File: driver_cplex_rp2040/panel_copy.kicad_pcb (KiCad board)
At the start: 6 copper layers, 40.2 x 40.2 mm, 391 parts, among them J1 Conn_01x05, J2 Conn_01x05, J5 USB_C_Receptacle_USB2.0, U2 AP2112K-3.3, U5 RP2040, U6 W25Q128JVS

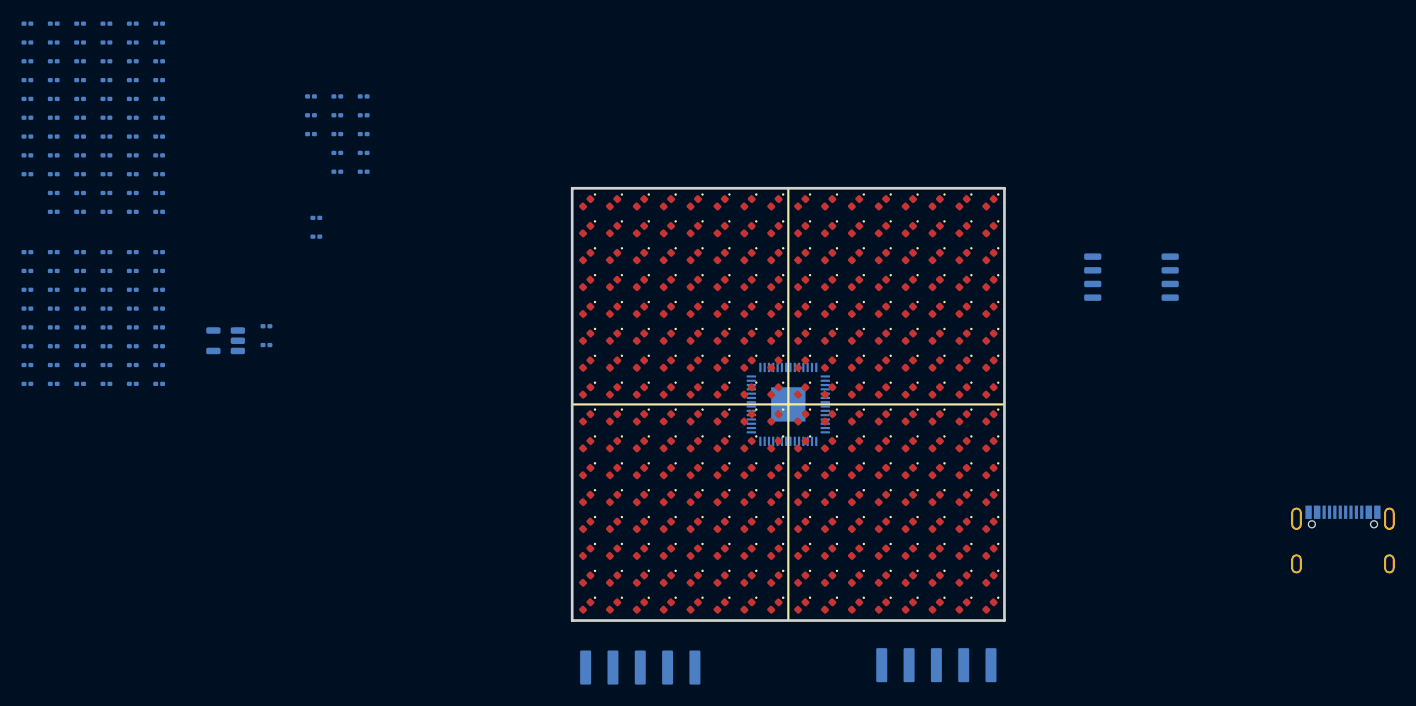
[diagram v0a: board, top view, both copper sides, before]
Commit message: Added charlie plexed version of single panel design.
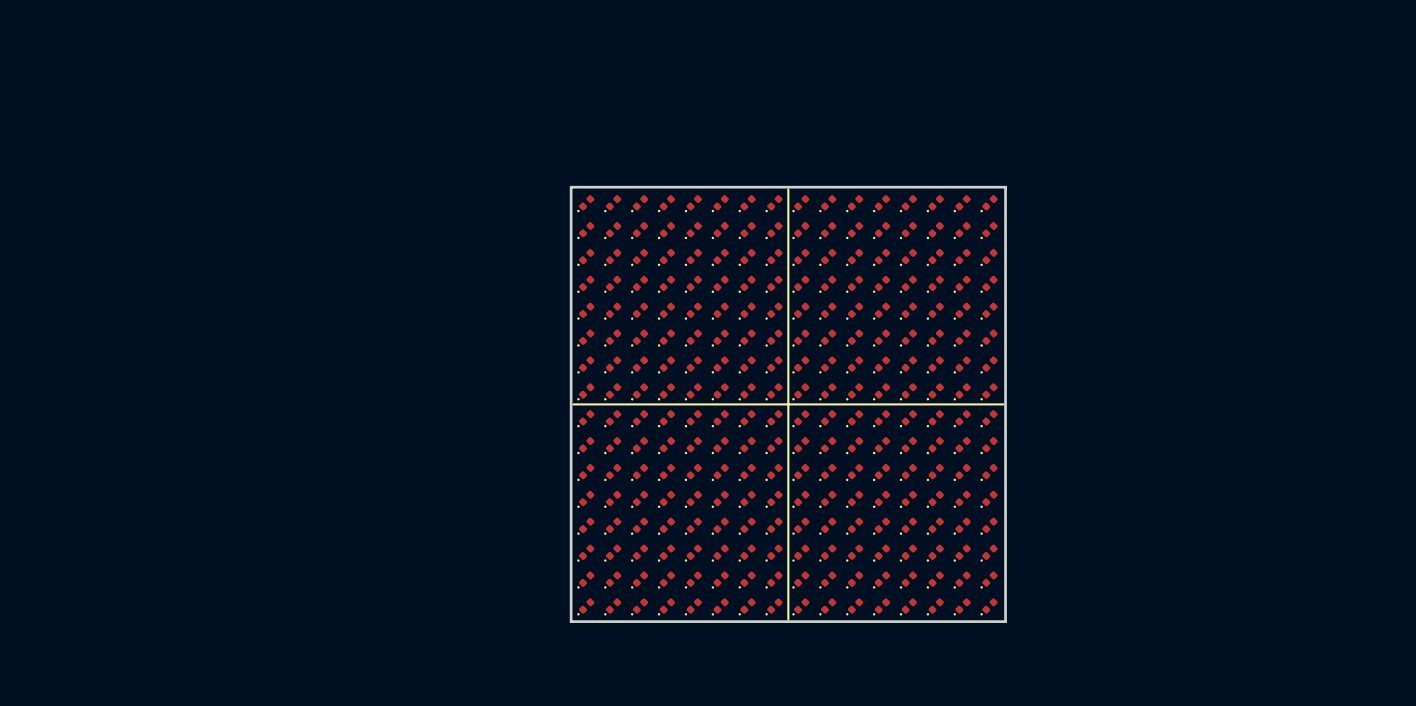
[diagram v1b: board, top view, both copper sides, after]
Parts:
- removed C1, C2: 20pF, panel_custom:C_0201_0603Metric
- removed C10, C11, C12, C13, C3, C4, C48, C49, C6, C7: 0.1uF, panel_custom:C_0201_0603Metric
- removed C17, C18, C19, C20, C21, C22, C23, C24, C25, C26, C27, C28, C29, C30, C31, C32: 200pF, panel_custom:C_0201_0603Metric
- removed C38, C47: 22uF, panel_custom:C_0201_0603Metric
- removed C5, C8, C9: 1uF, panel_custom:C_0201_0603Metric
- removed J1, J2: Conn_01x05, panel_custom:PinHeader_1x5_M20-8890545R
- removed J5: USB_C_Receptacle_USB2.0, Connector_USB:USB_C_Receptacle_G-Switch_GT-USB-7010ASV
- removed R1, R17, R18, R19, R2, R20, R3, R4, R70, R71, R72, R73, R86, R87, R88, R89: 2k, panel_custom:R_0201_0603Metric
- removed R10, R101, R12, R14, R16, R26, R28, R30, R32, R79, R81, R83, R85, R95, R97, R99: 10k, panel_custom:R_0201_0603Metric
- removed R100, R11, R13, R15, R21, R22, R23, R24, R25, R27, R29, R31, R5, R6, R7, R74, R75, R76, R77, R78, R8, R80, R82, R84, R9, R90, R91, R92, R93, R94, R96, R98: 4.5k, panel_custom:R_0201_0603Metric
- removed R33, R34, R35, R36, R41, R42, R43, R44, R49, R50, R51, R52, R57, R58, R59, R60: 1k, panel_custom:R_0201_0603Metric
- removed R37, R38, R39, R40, R45, R46, R47, R48, R53, R54, R55, R56, R61, R62, R63, R64: 100, panel_custom:R_0201_0603Metric
- removed U2: AP2112K-3.3, Package_TO_SOT_SMD:SOT-23-5
- removed U5: RP2040, Package_DFN_QFN:QFN-56-1EP_7x7mm_P0.4mm_EP3.2x3.2mm
- removed U6: W25Q128JVS, Package_SO:SOIC-8_5.23x5.23mm_P1.27mm
- moved D185 22.4 mm to (88.8, 51.2), turned to 45 degrees
- moved D186 22.4 mm to (88.8, 53.8), turned to 45 degrees
- moved D187 22.4 mm to (88.8, 56.2), turned to 45 degrees
- moved D188 22.4 mm to (88.8, 58.8), turned to 45 degrees
- moved D189 22.4 mm to (88.8, 61.2), turned to 45 degrees
- moved D190 22.4 mm to (88.8, 63.8), turned to 45 degrees
- moved D191 22.4 mm to (88.8, 66.2), turned to 45 degrees
- moved D192 22.4 mm to (88.8, 68.8), turned to 45 degrees
- moved D193 22.4 mm to (71.2, 71.2), turned to 45 degrees
- moved D194 22.4 mm to (71.2, 73.8), turned to 45 degrees
- moved D195 22.4 mm to (71.2, 76.2), turned to 45 degrees
- moved D196 22.4 mm to (71.2, 78.8), turned to 45 degrees
- moved D197 22.4 mm to (71.2, 81.2), turned to 45 degrees
- moved D198 22.4 mm to (71.2, 83.8), turned to 45 degrees
- moved D199 22.4 mm to (71.2, 86.2), turned to 45 degrees
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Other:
- board size 40.2 x 40.2 mm -> 40.4 x 40.4 mm
